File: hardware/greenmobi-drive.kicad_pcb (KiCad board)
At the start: 2 copper layers, 100 x 100 mm, 147 parts, among them J1 GND, J10 Motor NTC, J2 Encoder/Hall, J3 UBAT, J4 USB_C_Receptacle_USB2.0_14P, J5 CAN, J6 Debug, J7 Phase_OUT, J8 Phase_OUT, J9 Phase_OUT, Q3 AGM015N10LL, Q4 AGM015N10LL, Q5 AGM015N10LL, Q6 AGM015N10LL, Q7 AGM015N10LL, Q8 AGM015N10LL, SW1 BOOT, SW2 RESET, U1 BMI323, U10 TPS54202DDC, U11 LM5163DDA, U12 AMS1117-3.3, U2 TJA1051T-3, U3 STM32F405RGTx, U4 IRS21867S, U5 INA240A2D, U6 IRS21867S, U7 INA240A2D, U8 IRS21867S, U9 INA240A2D, Y1 8MHz

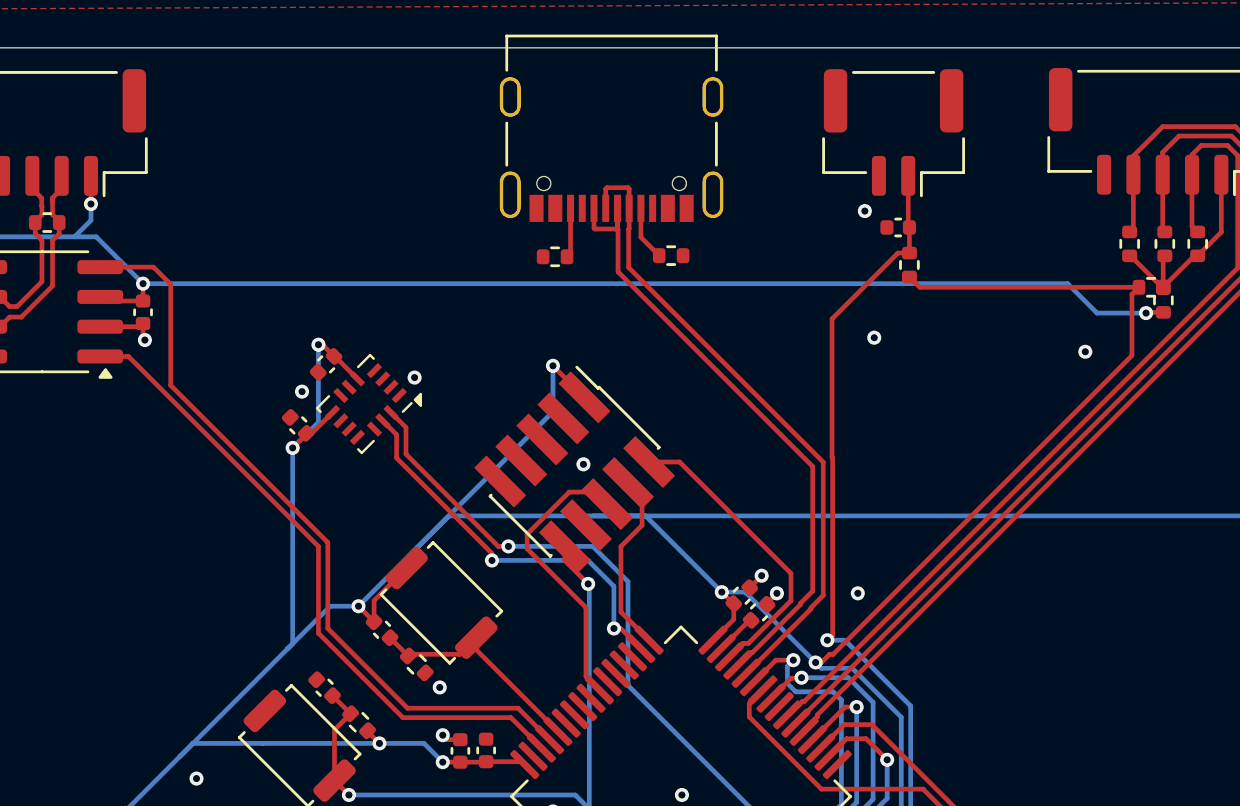
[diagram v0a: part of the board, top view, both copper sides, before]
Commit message: Move traces away from USB
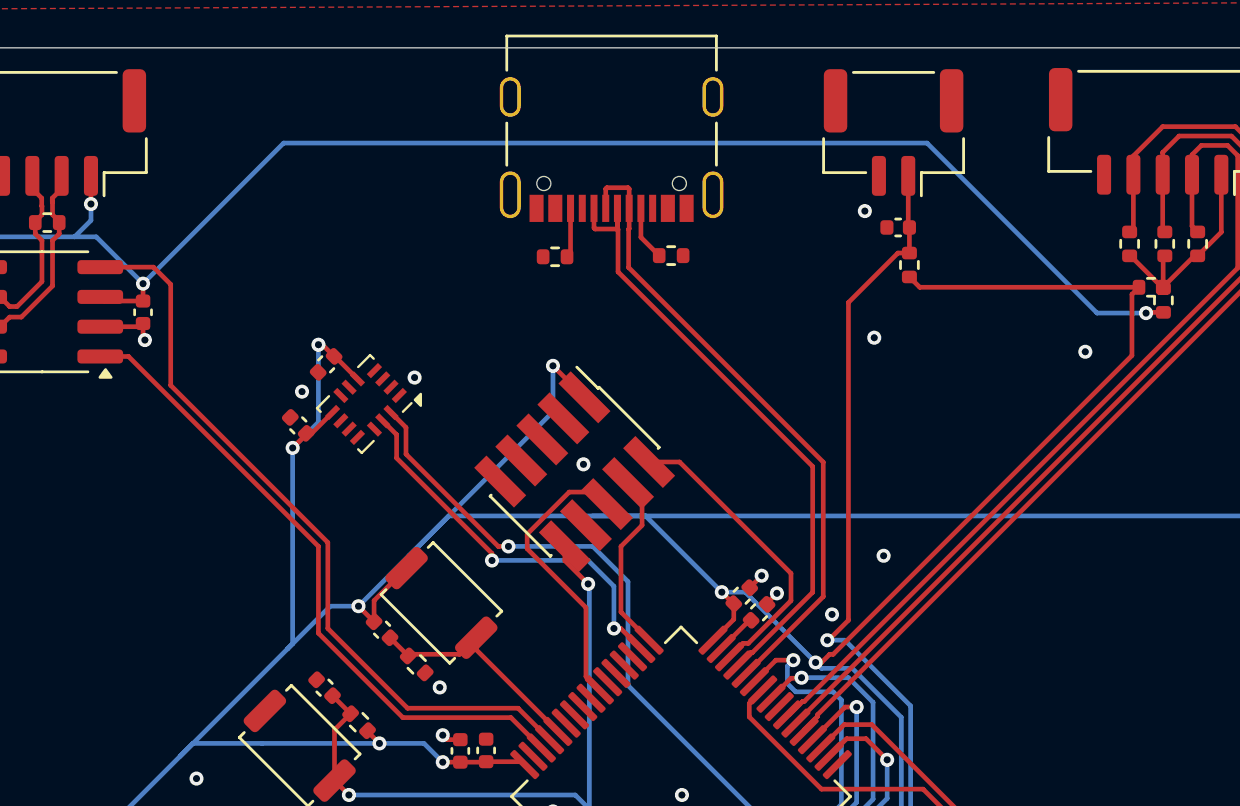
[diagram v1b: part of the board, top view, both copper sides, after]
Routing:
- net +5V: track 100.3 -> 105.2 mm
- net GND: vias 70 -> 71
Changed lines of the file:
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@@
 	)
 	(via
+		(at 163.9 70.2)
+		(size 0.6)
+		(drill 0.3)
+		(layers "F.Cu" "B.Cu")
+		(free yes)
+		(net 1)
+	)
+	(via
 		(at 126.15 59.2)
 		(size 0.6)
@@
 	)
 	(via
-		(at 165 69.3)
+		(at 166.1 67.7)
 		(size 0.6)
 		(drill 0.3)
@@
 	)
 	(segment
-		(start 154.775 53.780001)
-		(end 154.75 53.755001)
+		(start 163.075 63.893198)
+		(end 154.775 55.593198)
 		(width 0.2)
 		(layer "F.Cu")
@@
 	)
 	(segment
-		(start 163.075 69.204038)
-		(end 163.075 63.893198)
+		(start 154.775 53.780001)
+		(end 154.75 53.755001)
 		(width 0.2)
 		(layer "F.Cu")
@@
 	)
 	(segment
-		(start 154.75 53.717)
-		(end 154.75 52.885)
+		(start 154.775 55.593198)
+		(end 154.775 53.780001)
 		(width 0.2)
 		(layer "F.Cu")
@@
 	)
 	(segment
-		(start 159.883022 72.36066)
-		(end 160.407499 71.836183)
+		(start 154.75 53.717)
+		(end 154.75 52.885)
 		(width 0.2)
 		(layer "F.Cu")
@@
 	)
 	(segment
-		(start 163.075 63.893198)
-		(end 154.775 55.593198)
+		(start 163.075 69.256186)
+		(end 163.075 63.893198)
 		(width 0.2)
 		(layer "F.Cu")
@@
 	)
 	(segment
-		(start 162.551 69.780186)
-		(end 162.551 69.728038)
+		(start 159.883022 72.36066)
+		(end 160.407499 71.836183)
 		(width 0.2)
 		(layer "F.Cu")
@@
 	)
 	(segment
-		(start 162.551 69.728038)
-		(end 163.075 69.204038)
-		(width 0.2)
-		(layer "F.Cu")
-		(net 15)
-	)
-	(segment
 		(start 160.407499 71.836183)
 		(end 160.495003 71.836183)
@@
 	)
 	(segment
-		(start 154.775 55.593198)
-		(end 154.775 53.780001)
-		(width 0.2)
-		(layer "F.Cu")
-		(net 15)
-	)
-	(segment
 		(start 160.495003 71.836183)
-		(end 162.551 69.780186)
+		(end 163.075 69.256186)
 		(width 0.2)
 		(layer "F.Cu")
@@
 	)
 	(segment
-		(start 155.25 53.755001)
-		(end 155.25 52.885)
+		(start 160.664625 72.286163)
+		(end 160.681391 72.286163)
 		(width 0.2)
 		(layer "F.Cu")
@@
 	)
 	(segment
-		(start 160.681391 72.286163)
-		(end 163.00098 69.966574)
+		(start 163.525 69.442554)
+		(end 163.525 63.706802)
 		(width 0.2)
 		(layer "F.Cu")
@@
 	)
 	(segment
-		(start 163.00098 69.914452)
-		(end 163.525 69.390432)
-		(width 0.2)
-		(layer "F.Cu")
-		(net 29)
-	)
-	(segment
-		(start 155.225 55.406802)
-		(end 155.225 53.780001)
-		(width 0.2)
-		(layer "F.Cu")
-		(net 29)
-	)
-	(segment
-		(start 160.664625 72.286163)
-		(end 160.681391 72.286163)
-		(width 0.2)
-		(layer "F.Cu")
-		(net 29)
-	)
-	(segment
 		(start 154.25 52.053)
 		(end 154.25 52.885)
@@
 	)
 	(segment
-		(start 163.525 69.390432)
-		(end 163.525 63.706802)
+		(start 155.225 55.406802)
+		(end 155.225 53.780001)
 		(width 0.2)
 		(layer "F.Cu")
@@
 	)
 	(segment
-		(start 163.00098 69.966574)
-		(end 163.00098 69.914452)
+		(start 155.25 53.755001)
+		(end 155.25 52.885)
 		(width 0.2)
 		(layer "F.Cu")
@@
 	)
 	(segment
-		(start 160.236575 72.714213)
-		(end 160.664625 72.286163)
+		(start 160.681391 72.286163)
+		(end 163.525 69.442554)
 		(width 0.2)
 		(layer "F.Cu")
@@
 	)
 	(segment
+		(start 160.236575 72.714213)
+		(end 160.664625 72.286163)
+		(width 0.2)
+		(layer "F.Cu")
+		(net 29)
+	)
+	(segment
 		(start 155.201 52.004)
 		(end 154.299 52.004)
@@
 	)
 	(segment
-		(start 163.926 71.121878)
-		(end 163.926 63.540702)
+		(start 164.6 70.447878)
+		(end 164.6 56.9)
 		(width 0.2)
 		(layer "F.Cu")
@@
 	)
 	(segment
-		(start 167.2 54.79)
-		(end 167.2 53.7)
+		(start 164.6 56.9)
+		(end 166.71 54.79)
 		(width 0.2)
 		(layer "F.Cu")
@@
 	)
 	(segment
-		(start 167.15 53.65)
-		(end 167.2 53.7)
+		(start 166.71 54.79)
+		(end 167.2 54.79)
 		(width 0.2)
 		(layer "F.Cu")
@@
 	)
 	(segment
-		(start 163.747878 71.3)
-		(end 163.926 71.121878)
+		(start 167.2 54.79)
+		(end 167.2 53.7)
 		(width 0.2)
 		(layer "F.Cu")
@@
 	)
 	(segment
-		(start 163.9 57.6)
-		(end 166.71 54.79)
+		(start 167.15 53.65)
+		(end 167.2 53.7)
 		(width 0.2)
 		(layer "F.Cu")
@@
 	)
 	(segment
-		(start 166.71 54.79)
-		(end 167.2 54.79)
+		(start 163.7 71.3)
+		(end 163.747878 71.3)
 		(width 0.2)
 		(layer "F.Cu")
@@
 	)
 	(segment
-		(start 163.9 63.514702)
-		(end 163.9 57.6)
-		(width 0.2)
-		(layer "F.Cu")
-		(net 50)
-	)
-	(segment
 		(start 163.749943 83.15)
 		(end 162.293146 83.15)
@@
 	)
 	(segment
-		(start 163.926 63.540702)
-		(end 163.9 63.514702)
-		(width 0.2)
-		(layer "F.Cu")
-		(net 50)
-	)
-	(segment
-		(start 163.7 71.3)
-		(end 163.747878 71.3)
+		(start 163.747878 71.3)
+		(end 164.6 70.447878)
 		(width 0.2)
 		(layer "F.Cu")
@@
 	)
 	(segment
-		(start 177.290001 57.35)
-		(end 175.2 57.35)
+		(start 167.95 50.1)
+		(end 140.516621 50.1)
 		(width 0.2)
 		(layer "B.Cu")
@@
 	)
 	(segment
+		(start 140.516621 50.1)
+		(end 134.520524 56.096097)
+		(width 0.2)
+		(layer "B.Cu")
+		(net 61)
+	)
+	(segment
+		(start 177.290001 57.35)
+		(end 175.2 57.35)
+		(width 0.2)
+		(layer "B.Cu")
+		(net 61)
+	)
+	(segment
 		(start 132.3 53.399)
 		(end 131.6 54.099)
@@
 	)
 	(segment
+		(start 175.2 57.35)
+		(end 167.95 50.1)
+		(width 0.2)
+		(layer "B.Cu")
+		(net 61)
+	)
+	(segment
 		(start 124.701 66.299)
 		(end 119.3 71.7)
@@
 		(width 0.2)
 		(layer "B.Cu")
-		(net 61)
-	)
-	(segment
-		(start 173.946097 56.096097)
-		(end 134.520524 56.096097)
-		(width 0.2)
-		(layer "B.Cu")
-		(net 61)
-	)
-	(segment
-		(start 175.2 57.35)
-		(end 173.946097 56.096097)
-		(width 0.2)
-		(layer "B.Cu")

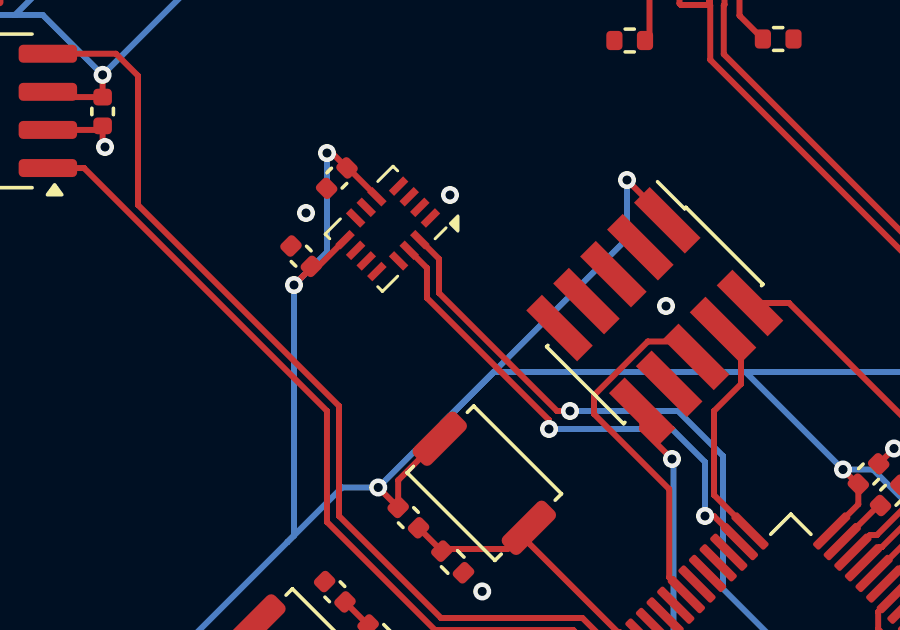
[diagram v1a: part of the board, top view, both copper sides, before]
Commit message: Add missing I2C pullups
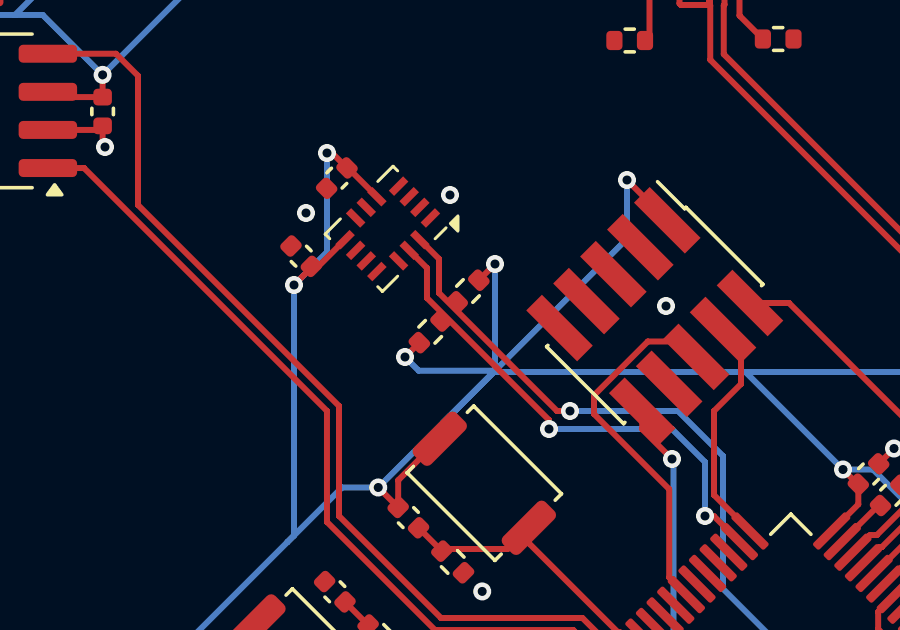
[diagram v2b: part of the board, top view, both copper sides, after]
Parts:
- added R15: 5.1k, Resistor_SMD:R_0402_1005Metric, F.Cu at (145.4, 64.7)
- added R49: 5.1k, Resistor_SMD:R_0402_1005Metric, F.Cu at (146.7, 63.3)
- L1, L2, L3, L4: value L_Ferrite -> 1k@100MHz
- Q3, Q4, Q5, Q6, Q7, Q8: value AGM015N10LL -> IPT015N10N5
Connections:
- net /SCL renamed /IMU_SCL
- net /SDA renamed /IMU_SDA
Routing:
- net +3.3V: track 330.4 -> 338.7 mm, vias 23 -> 25

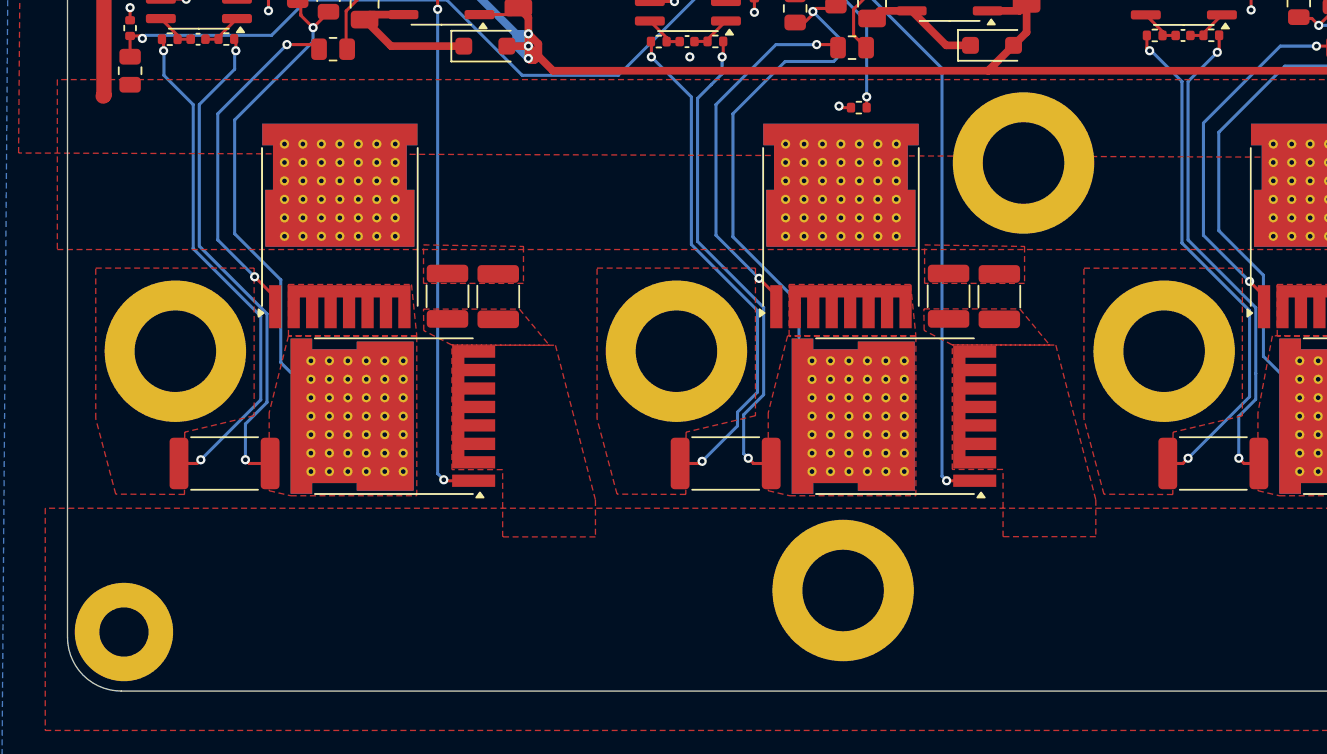
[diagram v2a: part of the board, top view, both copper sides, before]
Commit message: Change power connections to pads instead of holes
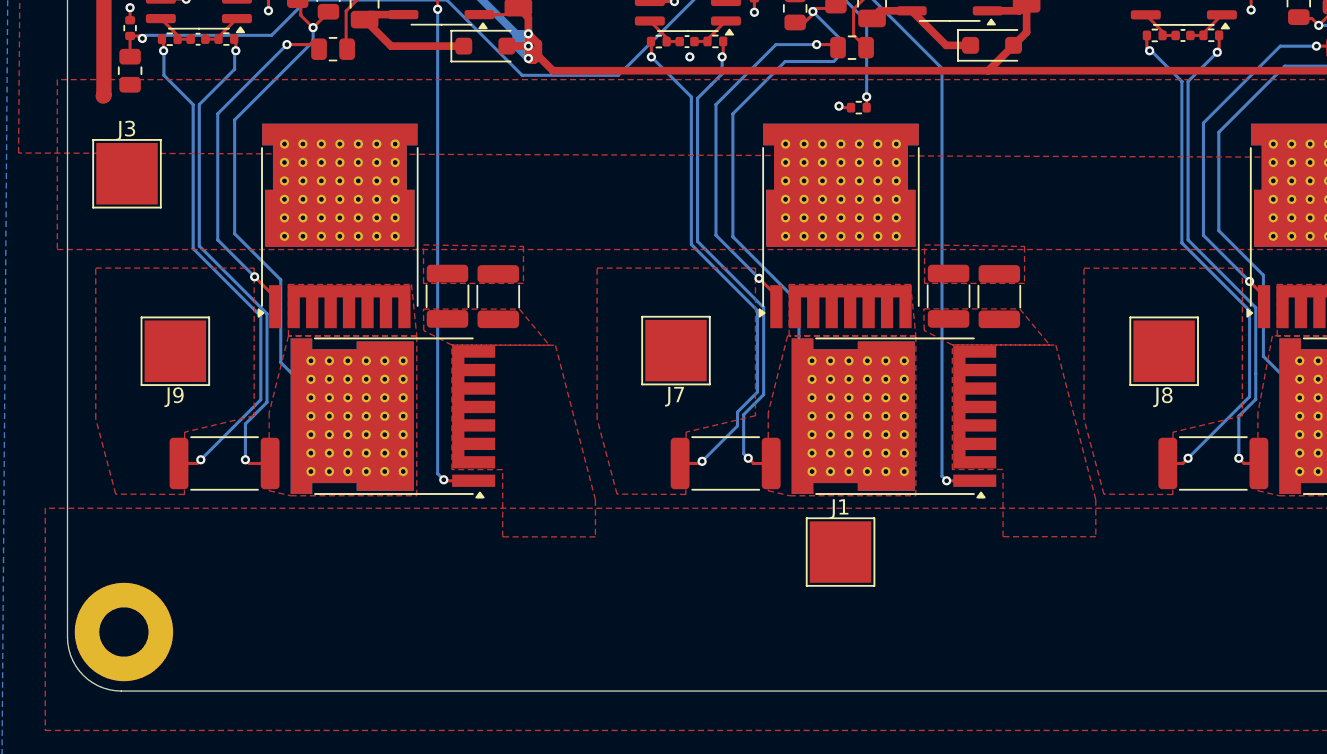
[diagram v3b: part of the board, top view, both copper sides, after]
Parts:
- J1, J3, J7, J8, J9: footprint MountingHole:MountingHole_5.3mm_M5_DIN965_Pad -> TestPoint:TestPoint_Pad_4.0x4.0mm
- moved J3 58.3 mm to (97.8, 112.4)
- moved J1 2.51 mm to (144.2, 137.0)
